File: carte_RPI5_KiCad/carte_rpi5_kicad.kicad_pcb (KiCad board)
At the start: 2 copper layers, 134.6 x 58.9 mm, 26 parts, among them J1 Conn_01x03, J10 RPI5_40pins, J2 Conn_01x03, J3 Conn_01x03, J4 Conn_01x03, J5 Conn_01x03, J6 Conn_01x03, J7 Conn_01x03, J8 Conn_01x03, J9 XT60-M, SW1 SW_SPDT

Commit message: modif PCB 06/02
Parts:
- removed G***: LOGO, LOGO
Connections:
- J10 pad 1: 3.3V -> 5V
- J10 pad 10: unconnected-(J10-Pin_10-Pad10) -> GND
- J10 pad 13: unconnected-(J10-Pin_13-Pad13) -> GND
- J10 pad 14: GND -> unconnected-(J10-Pin_14-Pad14)
- J10 pad 17: 3.3V -> unconnected-(J10-Pin_17-Pad17)
- J10 pad 18: unconnected-(J10-Pin_18-Pad18) -> 3.3V
- J10 pad 19: unconnected-(J10-Pin_19-Pad19) -> GND
- J10 pad 2: 5V -> 3.3V
- J10 pad 20: GND -> unconnected-(J10-Pin_20-Pad20)
- J10 pad 25: GND -> unconnected-(J10-Pin_25-Pad25)
- J10 pad 26: unconnected-(J10-Pin_26-Pad26) -> GND
- J10 pad 29: unconnected-(J10-Pin_29-Pad29) -> GND
- J10 pad 3: SDA -> 5V
- J10 pad 30: GND -> unconnected-(J10-Pin_30-Pad30)
- J10 pad 33: unconnected-(J10-Pin_33-Pad33) -> GND
- J10 pad 34: GND -> unconnected-(J10-Pin_34-Pad34)
- J10 pad 39: GND -> unconnected-(J10-Pin_39-Pad39)
- J10 pad 4: 5V -> SDA
- J10 pad 40: unconnected-(J10-Pin_40-Pad40) -> GND
- J10 pad 5: SCL -> GND
- J10 pad 6: GND -> SCL
- J10 pad 9: GND -> unconnected-(J10-Pin_9-Pad9)
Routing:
- net 3.3V: track 212.8 -> 242.5 mm, vias 4 -> 2
- net SCL: track 141.8 -> 113.5 mm
- net SDA: track 152.5 -> 132.6 mm
- net 5V: track 204.7 -> 207.6 mm
- net PWM6: track 29.6 -> 32.0 mm
- net PWM3: track 81.5 -> 79.2 mm
- net PWM5: track 29.5 -> 31.3 mm
- net PWM2: track 92.4 -> 94.0 mm
- net PWM0: track 86.5 -> 85.5 mm
- net PWM1: track 90.5 -> 91.4 mm
- net GND: track 0.00 -> 0.84 mm, vias 3 -> 4

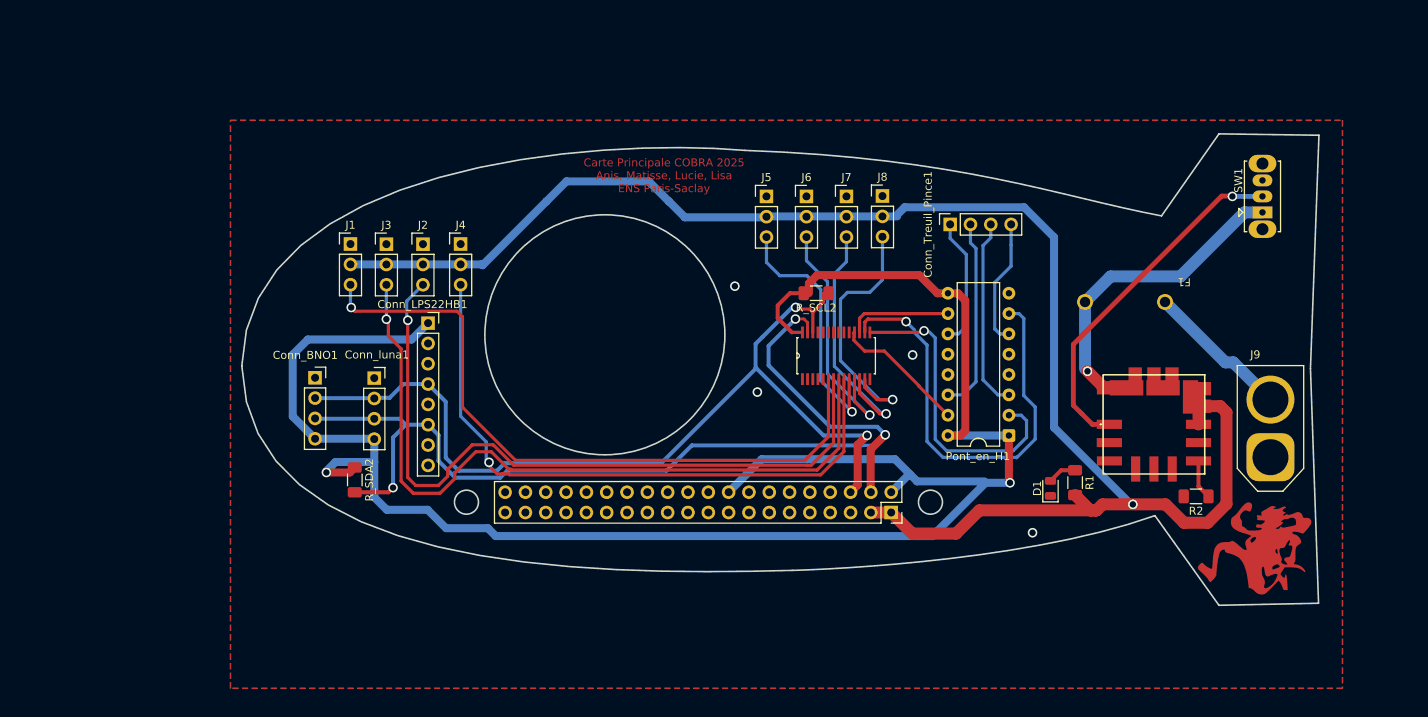
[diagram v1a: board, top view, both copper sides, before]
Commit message: modif_PCB_ajout_resistance
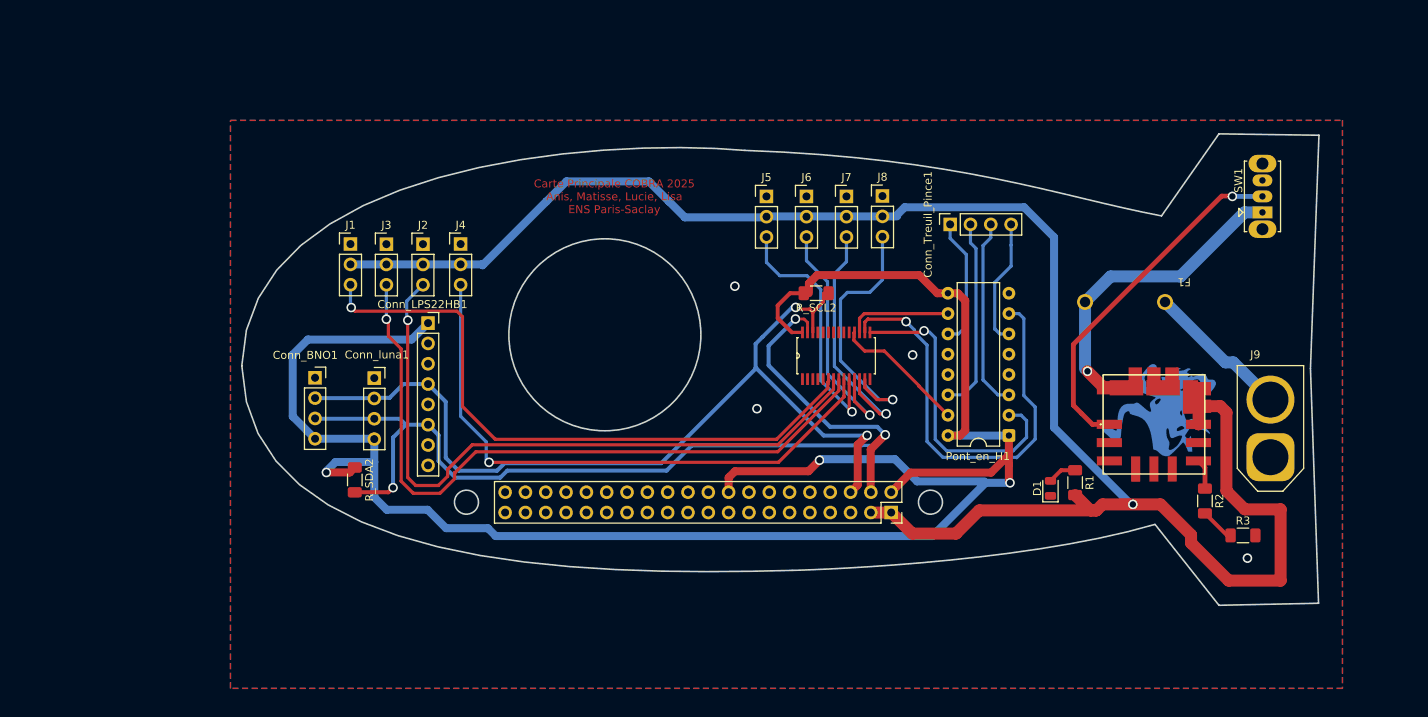
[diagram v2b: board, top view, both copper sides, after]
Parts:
- added R3: 40, Resistor_SMD:R_1206_3216Metric_Pad1.30x1.75mm_HandSolder, F.Cu at (187.6, 111.9)
- R2: value 1340 -> 1300
- moved ? 21.0 mm to (179.8, 96.3)
- moved R2 1.25 mm to (182.8, 107.6), turned to -90 degrees
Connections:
- R2 pad 2: GND -> Net-(R2-Pad2)
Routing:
- net 5V: track 207.6 -> 232.0 mm
- net 3.3V: track 242.5 -> 257.2 mm, vias 2 -> 3
- net PWM2: track 94.0 -> 87.8 mm
- net PWM1: track 91.4 -> 85.4 mm
- net PWM0: track 85.5 -> 79.5 mm
- net PWM3: track 79.2 -> 74.1 mm
- net Net-(R2-Pad2): track 0.00 -> 4.39 mm
- net Net-(Régulateur_de_tension1-TRIM): track 4.95 -> 3.79 mm
- net Net-(Régulateur_de_tension1-ON/OFF_CONTROL): track 45.0 -> 44.4 mm
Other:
- outline, holes or cut-outs redrawn

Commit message: Ajout_fichiers
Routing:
- net GND: vias 4 -> 5
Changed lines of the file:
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@@
+		(net 4)
+	)
+	(via
+		(at 169.32 74.86)
+		(size 1.2)
+		(drill 0.8)
+		(layers "F.Cu" "B.Cu")
 		(net 4)
 	)

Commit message: maj carte
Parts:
- removed Conn_BNO1: Conn_01x04_Pin, Connector_PinSocket_2.54mm:PinSocket_1x04_P2.54mm_Vertical
- added BMI055: 110990030, Connector:NS-Tech_Grove_1x04_P2mm_Vertical, F.Cu at (70.5, 75.0)
- added BMM350: Conn_01x09_Pin, Connector_PinSocket_2.54mm:PinSocket_1x09_P2.54mm_Vertical, F.Cu at (70.0, 100.6)
- added D3: Z2SMBxxx, Diode_SMD:D_SMB, F.Cu at (158.8, 112.5)
- added J12: XT60-M, Connector_AMASS:AMASS_XT60-F_1x02_P7.20mm_Vertical, F.Cu at (191.5, 103.6)
- F1: footprint librairie_empreintes:PTF-50 -> Fuse:Fuse_1206_3216Metric
- moved LPS22HB1 37.7 mm to (51.0, 100.1), turned to 180 degrees
- moved XT60 15.0 mm to (191.5, 87.1)
- moved MOT1 3.54 mm to (79.5, 75.0)
- moved MOT2 3.54 mm to (84.0, 75.0)
- moved MOT4 3.54 mm to (93.3, 75.0)
- moved MOT3 3.54 mm to (88.6, 75.0)
- moved SW 2.92 mm to (192.5, 70.0)
- moved ? 1.21 mm to (179.4, 97.4)
- renumbered R2 to 1300, R1 to 220, R_SCL2 to 4.7k, R_SDA2 to 4.7k, R3 to 40, Pont_en_H1 to L293D, Conn_LPS22HB1 to LPS22HB1, Conn_luna1 to LUNA, J1 to MOT1, J3 to MOT2, J2 to MOT3, J4 to MOT4, J5 to MOT5, J6 to MOT6, J7 to MOT7, J8 to MOT8, SW1 to SW, Conn_Treuil_Pince1 to Treuil, J9 to XT60
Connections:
- LUNA pad 4: 3.3V -> 5V
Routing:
- net 5V: track 232.0 -> 304.0 mm
- net SDA: track 132.6 -> 185.4 mm, vias 3 -> 5
- net SCL: track 113.5 -> 160.2 mm
- net 3.3V: track 257.2 -> 277.2 mm
- net Net-(Régulateur_de_tension1-VIN): track 40.5 -> 60.0 mm
- net Net-(J12-POS): track 19.2 -> 31.0 mm
- net PWM0: track 79.5 -> 75.4 mm
- net Net-(Régulateur_de_tension1-ON/OFF_CONTROL): track 44.4 -> 47.5 mm
- net PWM1: track 85.4 -> 87.5 mm
- net PWM2: track 87.8 -> 89.8 mm
- net PWM3: track 74.1 -> 73.1 mm
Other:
- board size 134.6 x 58.9 mm -> 153.6 x 68.2 mm
- board text added: "5V"
- board text added: "GND"
- board text added: "PWM"

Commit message: modif carte_dirigeable
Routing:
- net PWM1: track 87.5 -> 76.2 mm
- net PWM2: track 89.8 -> 82.5 mm
- net PWM0: track 75.4 -> 79.4 mm
- net PWM3: track 73.1 -> 73.7 mm
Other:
- board size 153.6 x 68.2 mm -> 153.6 x 69 mm

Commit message: modif2_carte_dirigeable
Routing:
- net NC: track 0.00 -> 7.62 mm
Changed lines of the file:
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@@
 		(net "PWM6")
+	)
+	(segment
+		(start 70 82.84)
+		(end 70 90.46)
+		(width 1)
+		(layer "F.Cu")
+		(net "NC")
 	)
 	(zone

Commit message: yes
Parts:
- renumbered J12 to XT60
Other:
- board text added: "PCA9685PW_118"
- board text added: "XT60"
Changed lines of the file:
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@@
 			(layer "F.Fab")
 		)
-		(fp_text user "${REFERENCE}"
+		(fp_text user "Connecteur Raspberry Pi 5"
 			(at 2.985 24.1 0)
-			(layer "F.Fab")
+			(layer "F.SilkS")
 			(effects
 				(font
@@
 		(descr "AMASS female XT60, through hole, vertical, https://www.tme.eu/Document/2d152ced3b7a446066e6c419d84bb460/XT60%20SPEC.pdf")
 		(tags "XT60 female vertical")
-		(property "Reference" "J12"
+		(property "Reference" "XT60"
 			(at 3.6 -5.3 90)
 			(layer "F.SilkS")
@@
 		(layer "Edge.Cuts")
 	)
+	(gr_text "PCA9685PW_118"
+		(at 184.5 106.76 0)
+		(layer "F.Cu")
+		(effects
+			(font
+				(size 1.27 1.27)
+			)
+		)
+	)
 	(gr_text "GND\n"
 		(at 76.5 75.5 0)
@@
 		)
 	)
+	(gr_text "PCA9685PW_118\n"
+		(at 136.99 94.37 0)
+		(layer "F.SilkS")
+		(effects
+			(font
+				(size 1 1)
+				(thickness 0.15)
+			)
+		)
+	)
+	(gr_text "XT60"
+		(at 186.07 84.23 90)
+		(layer "F.SilkS")
+		(effects
+			(font
+				(size 1 1)
+				(thickness 0.15)
+			)
+		)
+	)

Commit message: maj
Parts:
- added G***: LOGO, LOGO, F.Cu at (60.0, 97.9)
- added G***: LOGO, LOGO, F.Cu at (61.8, 103.8)
- added G***: LOGO, LOGO, F.Cu at (59.3, 87.6)
- moved BMI055 26.4 mm to (94.0, 63.1), turned to 0 degrees
- moved MOT4 21.1 mm to (148.5, 64.3)
- moved MOT5 21.1 mm to (153.5, 64.3)
- moved MOT6 21.1 mm to (158.5, 64.3)
- moved MOT7 21.1 mm to (163.0, 64.2)
- moved Treuil 17.6 mm to (168.3, 70.0)
- renumbered MOT1 to MOT0, MOT3 to MOT1, MOT4 to MOT3, MOT5 to MOT4, MOT6 to MOT5, MOT7 to MOT6, MOT8 to MOT7
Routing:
- net SCL: track 160.2 -> 190.9 mm
- net SDA: track 185.4 -> 215.5 mm
- net 3.3V: track 276.8 -> 305.0 mm
- net PWM7: track 33.0 -> 52.8 mm
- net Mot_treuil-: track 16.0 -> 34.8 mm
- net PWM6: track 32.0 -> 50.8 mm
- net Mot_treuil+: track 23.9 -> 41.2 mm
- net PWM5: track 31.3 -> 46.8 mm
- net Mot_pince-: track 24.1 -> 37.1 mm
- net Mot_pince+: track 16.2 -> 27.1 mm
- net PWM4: track 32.8 -> 42.5 mm
- net 5V: track 304.0 -> 300.2 mm, vias 1 -> 2
- net PWM2: track 82.5 -> 85.2 mm
- net PWM1: track 76.2 -> 78.7 mm
- net PWM0: track 79.4 -> 81.6 mm
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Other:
- board size 153.6 x 69 mm -> 156.2 x 67.4 mm
